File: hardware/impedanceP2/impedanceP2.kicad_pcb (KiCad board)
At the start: 2 copper layers, 98 x 79.6 mm, 73 parts, among them J1 RJ45, J2 RJ45, J3 USB, P1 JST-PH2, P2 CONN_24X2, P3 CONN_24X2, Q1 DMG2307L-7, Q2 DMG2307L-7, SW1 SWITCH_INV, U1 MC34063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

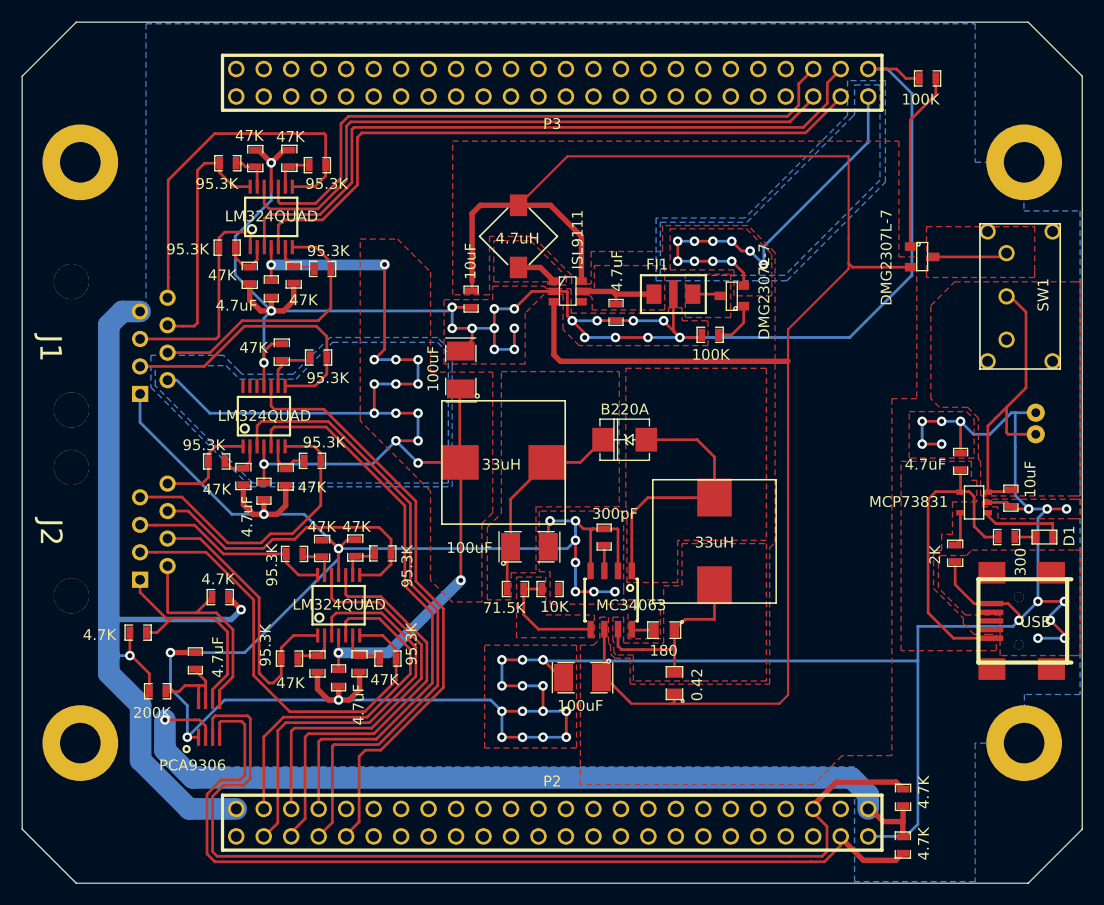
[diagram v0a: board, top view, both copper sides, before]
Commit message: updated to kicad 5 and cleanup
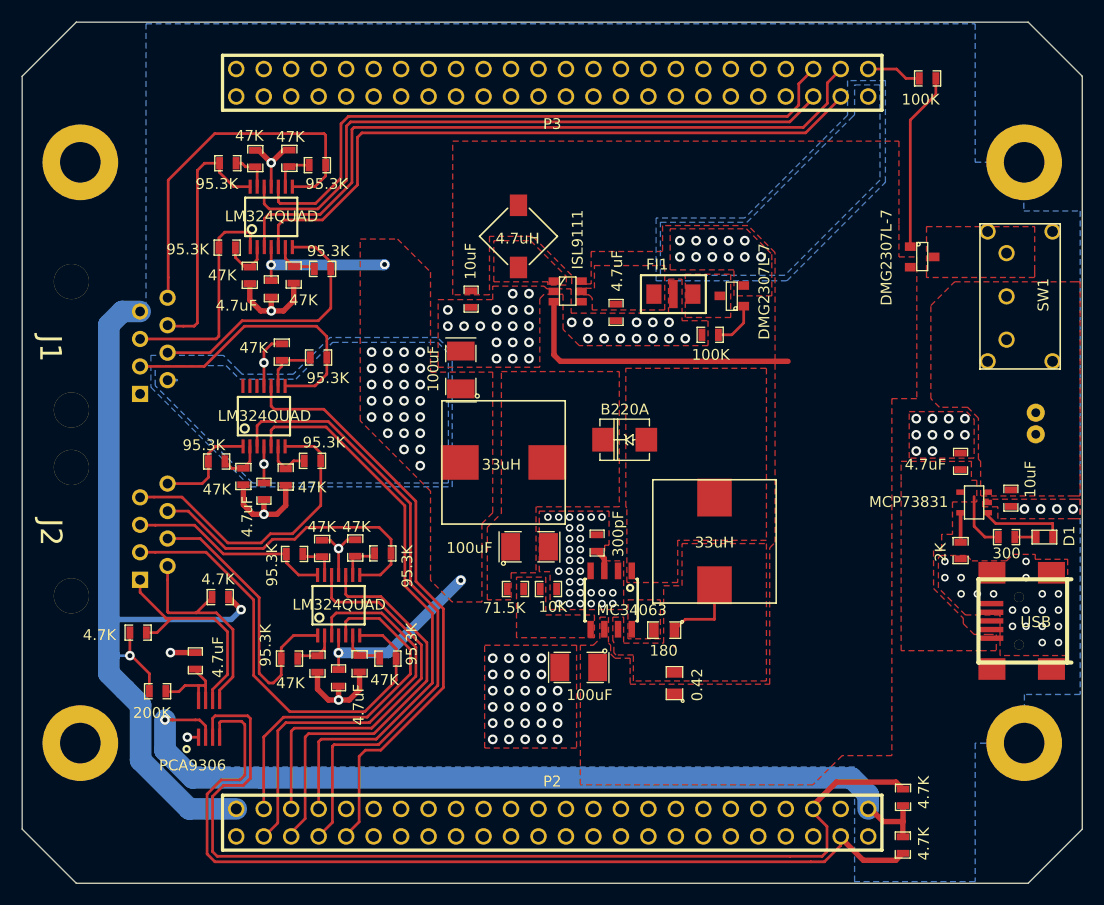
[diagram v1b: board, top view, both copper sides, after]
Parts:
- moved C6 1.01 mm to (102.5, 154.1)
- moved C7 0.85 mm to (104.2, 142.6)
- moved R2 0.56 mm to (137.8, 143.2)
- moved R8 0.15 mm to (99.7, 146.8)
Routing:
- net GND: track 495.7 -> 55.0 mm, vias 60 -> 130
- net /VMOS: track 164.4 -> 27.0 mm
- net /10VOUT: track 123.7 -> 36.0 mm, vias 17 -> 31
- net /5VOUT: track 115.9 -> 78.0 mm, vias 12 -> 13
- net /VBAT: track 27.8 -> 0.00 mm
- net N-0000023: track 24.4 -> 0.00 mm
- net +5V: track 29.4 -> 5.43 mm
- net N-0000034: track 21.9 -> 3.10 mm
- net N-0000024: track 18.2 -> 7.27 mm
- net N-0000022: track 10.8 -> 0.00 mm
- net N-0000028: track 7.77 -> 0.00 mm
- net N-00000113: track 6.85 -> 0.00 mm
- net N-0000029: track 3.80 -> 0.00 mm
- net N-0000030: track 2.57 -> 0.23 mm
- net N-0000025: track 2.27 -> 0.12 mm
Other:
- net class Default: via_dia 0.889 -> 0.9; via_drill 0.635 -> 0.5
- rule via_min_drill: 0.4 -> 0.3
- rule via_min_size: 0.8 -> 0.6
